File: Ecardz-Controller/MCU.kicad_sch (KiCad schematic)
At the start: 31 parts, among them J1 MEM2061-01-188-00-A, J2 Conn_01x04, J3 Conn_01x05, U1 STM32G0C1RETx

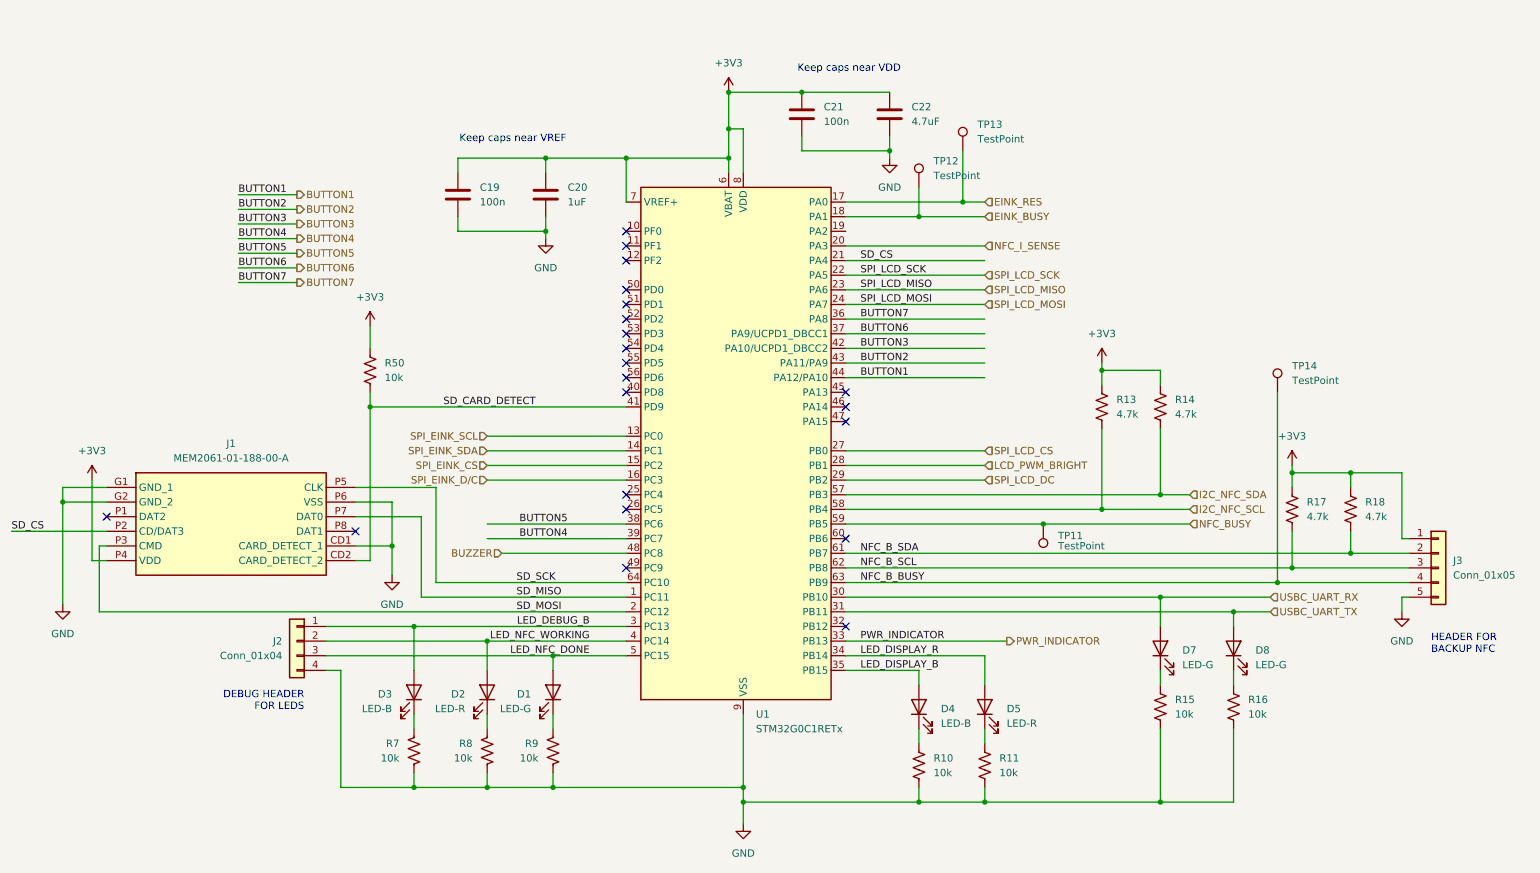
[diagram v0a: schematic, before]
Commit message: redid MCU connections from IOC file from FW team
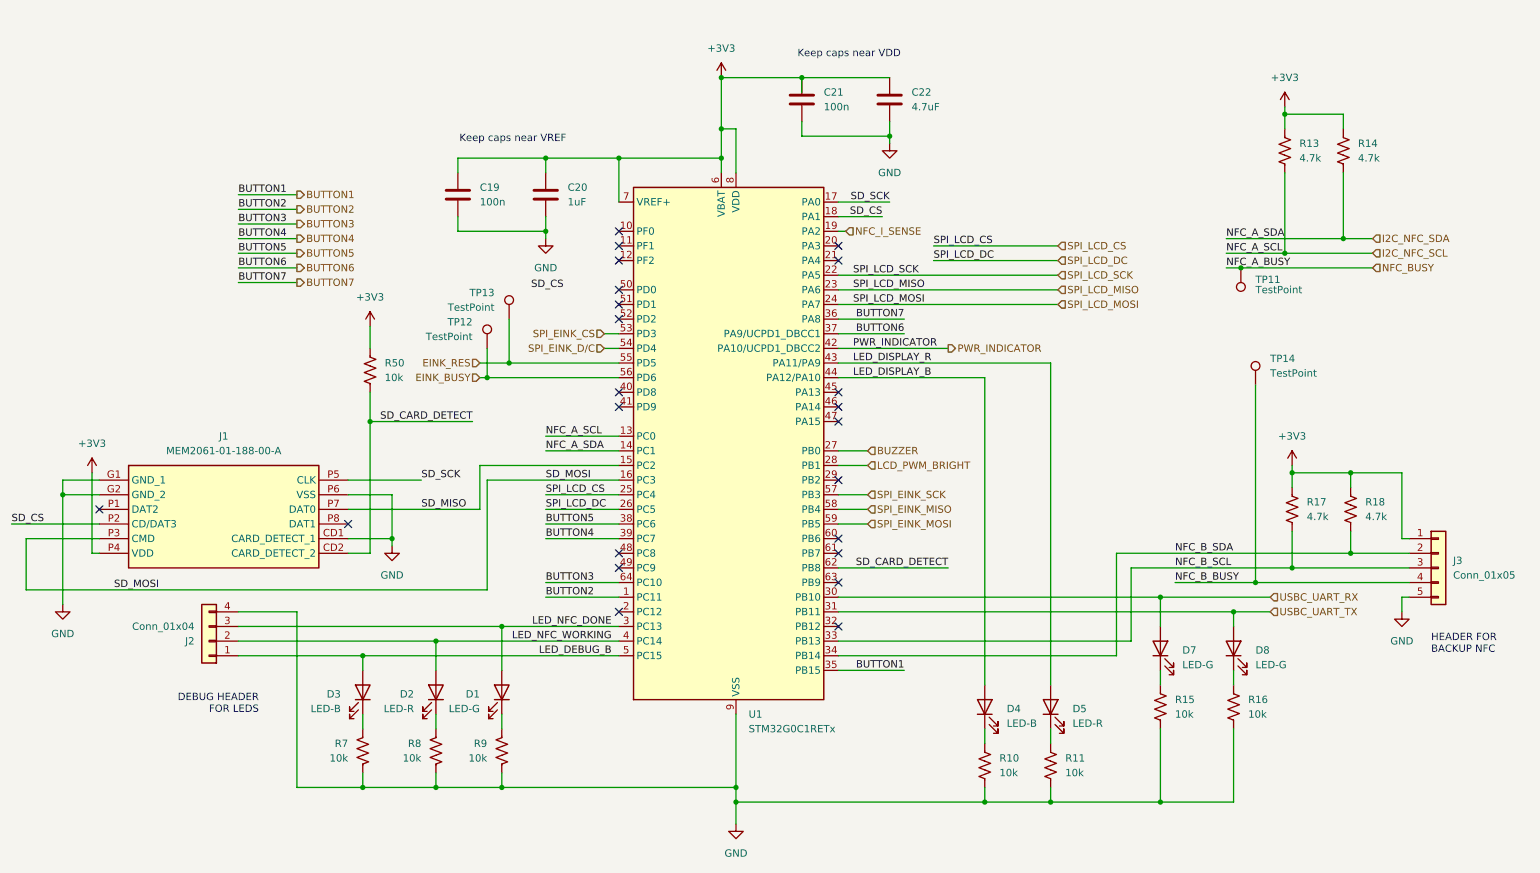
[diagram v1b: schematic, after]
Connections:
- net SPI_EINK_SCL is gone; now on net I2C_NFC_SCL: U1.13 (PC0)
- net SPI_EINK_SDA is gone; now on net I2C_NFC_SDA: U1.14 (PC1)
- net BUTTON1: now also U1.35 (PB15); no longer U1.44 (PA12/PA10)
- net BUTTON2: now also U1.1 (PC11); no longer U1.43 (PA11/PA9)
- net BUTTON3: now also U1.64 (PC10); no longer U1.42 (PA10/UCPD1_DBCC2)
- net BUZZER: now also U1.27 (PB0); no longer U1.48 (PC8)
- net EINK_BUSY: now also U1.56 (PD6); no longer U1.18 (PA1)
- net EINK_RES: now also U1.55 (PD5); no longer U1.17 (PA0)
- net I2C_NFC_SCL: no longer U1.58 (PB4)
- net I2C_NFC_SDA: no longer U1.57 (PB3)
- net LED_DEBUG_B: now also U1.5 (PC15); no longer U1.3 (PC13)
- net LED_DISPLAY_B: now also U1.44 (PA12/PA10); no longer U1.35 (PB15)
- net LED_DISPLAY_R: now also U1.43 (PA11/PA9); no longer U1.34 (PB14)
- net LED_NFC_DONE: now also U1.3 (PC13); no longer U1.5 (PC15)
- net NFC_BUSY: no longer U1.59 (PB5)
- net NFC_B_BUSY: no longer U1.63 (PB9)
- net NFC_B_SCL: now also U1.33 (PB13); no longer U1.62 (PB8)
- net NFC_B_SDA: now also U1.34 (PB14); no longer U1.61 (PB7)
- net NFC_I_SENSE: now also U1.19 (PA2); no longer U1.20 (PA3)
- net PWR_INDICATOR: now also U1.42 (PA10/UCPD1_DBCC2); no longer U1.33 (PB13)
- net SD_CARD_DETECT: now also U1.62 (PB8); no longer U1.41 (PD9)
- net SD_CS: now also U1.18 (PA1); no longer U1.21 (PA4)
- net SD_MISO: now also U1.15 (PC2); no longer U1.1 (PC11)
- net SD_MOSI: now also U1.16 (PC3); no longer U1.2 (PC12)
- net SD_SCK: now also U1.17 (PA0); no longer U1.64 (PC10)
- net SPI_EINK_CS: now also U1.53 (PD3); no longer U1.15 (PC2)
- net SPI_EINK_D/C: now also U1.54 (PD4); no longer U1.16 (PC3)
- net SPI_LCD_CS: now also U1.25 (PC4); no longer U1.27 (PB0)
- net SPI_LCD_DC: now also U1.26 (PC5); no longer U1.29 (PB2)
- new net SPI_EINK_MISO: U1.58 (PB4)
- new net SPI_EINK_MOSI: U1.59 (PB5)
- new net SPI_EINK_SCK: U1.57 (PB3)
- no-connect marks 21 -> 23
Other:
- moved on the sheet: C21, C22, D1, D2, D3, D4, D5, J1, R10, R11, R13, R14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

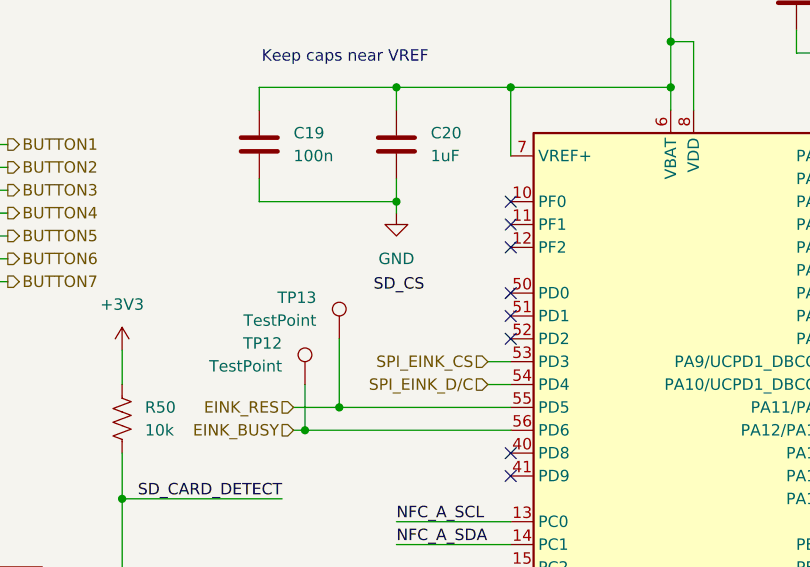
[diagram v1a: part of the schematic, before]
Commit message: updated layout for new mcu pin assignments
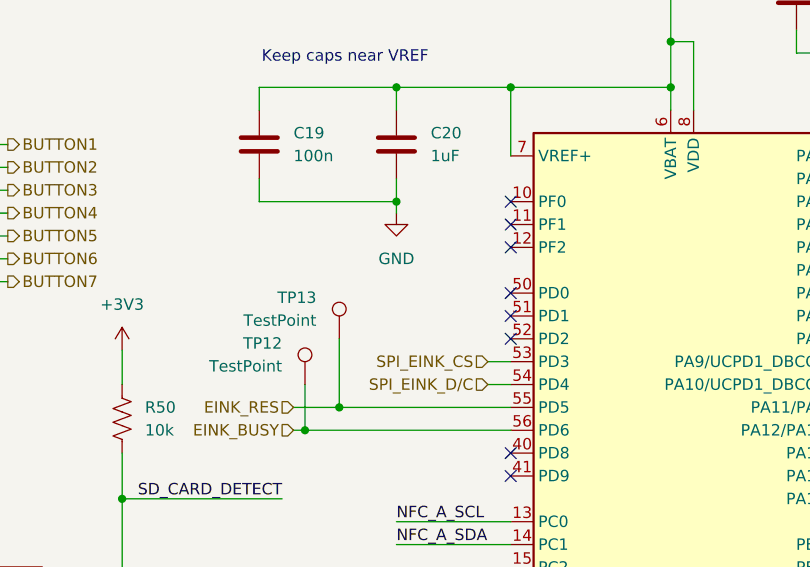
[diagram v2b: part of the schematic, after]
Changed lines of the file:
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@@
-		)
-	)
-	(label "SD_CS"
-		(at 106.68 60.96 0)
-		(fields_autoplaced yes)
-		(effects
-			(font
-				(size 1.27 1.27)
-			)
-			(justify left bottom)
 		)
 	)

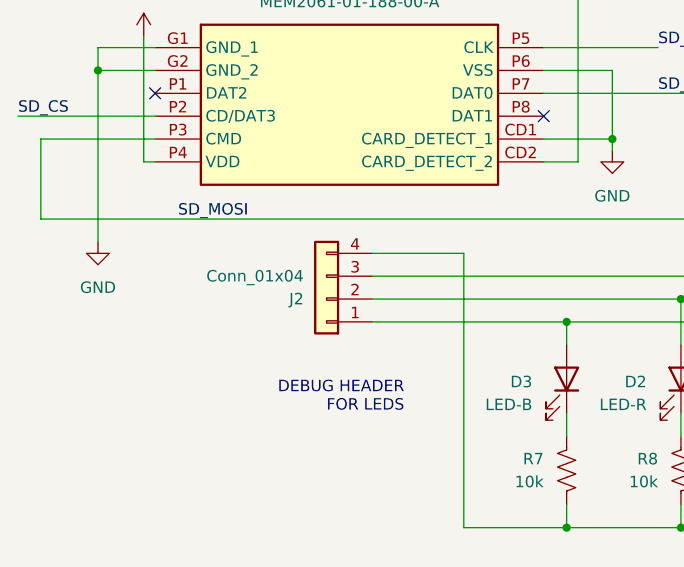
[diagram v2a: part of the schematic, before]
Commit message: changed headers to 90 degree angled headers
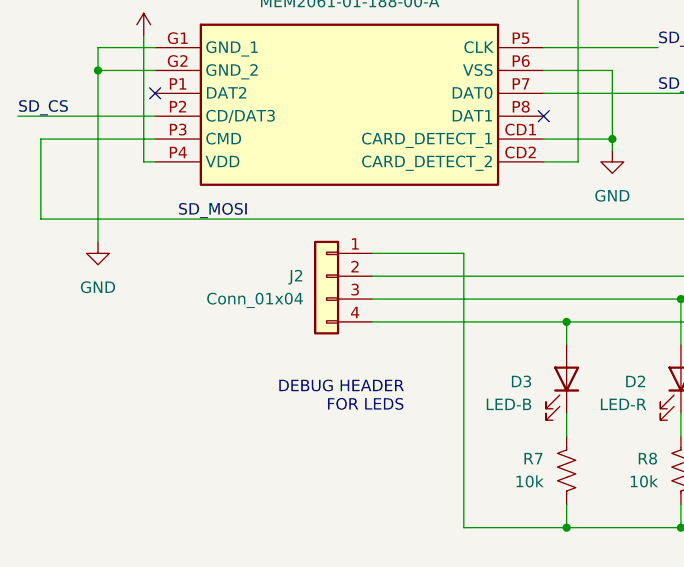
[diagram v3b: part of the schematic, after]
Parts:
- J2: footprint Connector_PinHeader_2.54mm:PinHeader_1x04_P2.54mm_Vertical -> Connector_PinHeader_2.54mm:PinHeader_1x04_P2.54mm_Horizontal
- J3: footprint Connector_PinHeader_2.54mm:PinHeader_1x05_P2.54mm_Vertical -> Connector_PinHeader_2.54mm:PinHeader_1x05_P2.54mm_Horizontal
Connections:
- net GND: now also J2.1 (Pin_1); no longer J2.4 (Pin_4)
- net LED_DEBUG_B: now also J2.4 (Pin_4); no longer J2.1 (Pin_1)
- net LED_NFC_DONE: now also J2.2 (Pin_2); no longer J2.3 (Pin_3)
- net LED_NFC_WORKING: now also J2.3 (Pin_3); no longer J2.2 (Pin_2)
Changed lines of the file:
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@@
+	)
+	(symbol
+		(lib_id "Connector_Generic:Conn_01x04")
+		(at 50.8 119.38 0)
+		(mirror y)
+		(unit 1)
+		(exclude_from_sim no)
+		(in_bom yes)
+		(on_board yes)
+		(dnp no)
+		(property "Reference" "J2"
+			(at 48.26 119.3799 0)
+			(effects
+				(font
+					(size 1.27 1.27)
+				)
+				(justify left)
+			)
+		)
+		(property "Value" "Conn_01x04"
+			(at 48.26 121.9199 0)
+			(effects
+				(font
+					(size 1.27 1.27)
+				)
+				(justify left)
+			)
+		)
+		(property "Footprint" "Connector_PinHeader_2.54mm:PinHeader_1x04_P2.54mm_Horizontal"
+			(at 50.8 119.38 0)
+			(effects
+				(font
+					(size 1.27 1.27)
+				)
+				(hide yes)
+			)
+		)
+		(property "Datasheet" ""
+			(at 50.8 119.38 0)
+			(effects
+				(font
+					(size 1.27 1.27)
+				)
+				(hide yes)
+			)
+		)
+		(property "Description" "Generic connector, single row, 01x04, script generated (kicad-library-utils/schlib/autogen/connector/)"
+			(at 50.8 119.38 0)
+			(effects
+				(font
+					(size 1.27 1.27)
+				)
+				(hide yes)
+			)
+		)
+		(property "Part Number" "61300411121"
+			(at 50.8 119.38 0)
+			(effects
+				(font
+					(size 1.27 1.27)
+				)
+				(hide yes)
+			)
+		)
+		(pin "2"
+		)
+		(pin "3"
+		)
+		(pin "4"
+		)
+		(pin "1"
+		)
+		(instances
+			(project "Ecardz-Controller"
+				(path "/74270717-a116-451e-ac88-5a07ab66056e/24ee7b4c-70f3-405d-afd9-1146a9b5f360"
+					(reference "J2")
+					(unit 1)
+				)
+			)
+		)
 	)
 	(symbol
@@
 				(path "/74270717-a116-451e-ac88-5a07ab66056e/24ee7b4c-70f3-405d-afd9-1146a9b5f360"
 					(reference "D8")
-					(unit 1)
-				)
-			)
-		)
-	)
-	(symbol
-		(lib_id "Connector_Generic:Conn_01x04")
-		(at 50.8 121.92 180)
-		(unit 1)
-		(exclude_from_sim no)
-		(in_bom yes)
-		(on_board yes)
-		(dnp no)
-		(property "Reference" "J2"
-			(at 48.26 121.9201 0)
-			(effects
-				(font
-					(size 1.27 1.27)
-				)
-				(justify left)
-			)
-		)
-		(property "Value" "Conn_01x04"
-			(at 48.26 119.3801 0)
-			(effects
-				(font
-					(size 1.27 1.27)
-				)
-				(justify left)
-			)
-		)
-		(property "Footprint" "Connector_PinHeader_2.54mm:PinHeader_1x04_P2.54mm_Vertical"
-			(at 50.8 121.92 0)
-			(effects
-				(font
-					(size 1.27 1.27)
-				)
-				(hide yes)
-			)
-		)
-		(property "Datasheet" ""
-			(at 50.8 121.92 0)
-			(effects
-				(font
-					(size 1.27 1.27)
-				)
-				(hide yes)
-			)
-		)
-		(property "Description" "Generic connector, single row, 01x04, script generated (kicad-library-utils/schlib/autogen/connector/)"
-			(at 50.8 121.92 0)
-			(effects
-				(font
-					(size 1.27 1.27)
-				)
-				(hide yes)
-			)
-		)
-		(property "Part Number" "61300411121"
-			(at 50.8 121.92 0)
-			(effects
-				(font
-					(size 1.27 1.27)
-				)
-				(hide yes)
-			)
-		)
-		(pin "2"
-		)
-		(pin "3"
-		)
-		(pin "4"
-		)
-		(pin "1"
-		)
-		(instances
-			(project "Ecardz-Controller"
-				(path "/74270717-a116-451e-ac88-5a07ab66056e/24ee7b4c-70f3-405d-afd9-1146a9b5f360"
-					(reference "J2")
 					(unit 1)
 				)
@@
 			)
 		)
-		(property "Footprint" "Connector_PinHeader_2.54mm:PinHeader_1x05_P2.54mm_Vertical"
+		(property "Footprint" "Connector_PinHeader_2.54mm:PinHeader_1x05_P2.54mm_Horizontal"
 			(at 264.16 109.22 0)
 			(effects

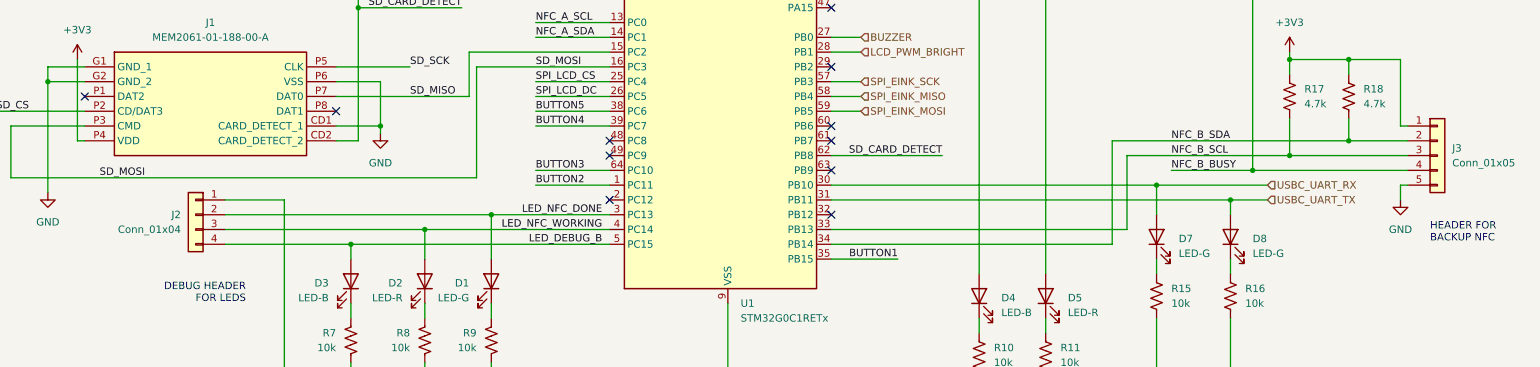
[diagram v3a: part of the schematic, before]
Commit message: moved headers to bottom of board, made J3 DNP
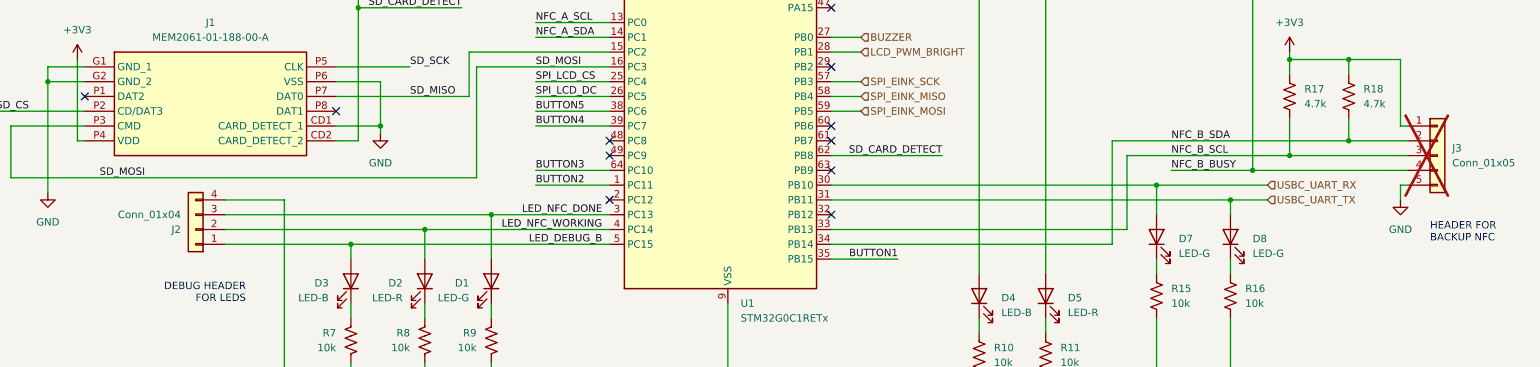
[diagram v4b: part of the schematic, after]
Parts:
- J3: now not fitted
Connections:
- net GND: now also J2.4 (Pin_4); no longer J2.1 (Pin_1)
- net LED_DEBUG_B: now also J2.1 (Pin_1); no longer J2.4 (Pin_4)
- net LED_NFC_DONE: now also J2.3 (Pin_3); no longer J2.2 (Pin_2)
- net LED_NFC_WORKING: now also J2.2 (Pin_2); no longer J2.3 (Pin_3)
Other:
- moved on the sheet: J2

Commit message: changed hole positions and fixed flex connector location in 3d model
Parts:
- added C54, C55, C56, C57, C58, C59, C60: 1uF, Capacitor_SMD:C_0603_1608Metric_Pad1.08x0.95mm_HandSolder, symbol Device:C
- added R51, R52, R53, R54, R55, R56, R57: 10k, Resistor_SMD:R_0603_1608Metric_Pad0.98x0.95mm_HandSolder, symbol Device:R_US
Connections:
- net BUTTON1: now also R51.2; no longer U1.35 (PB15)
- net BUTTON2: now also R52.2; no longer U1.1 (PC11)
- net BUTTON3: now also R53.2; no longer U1.64 (PC10)
- net BUTTON4: now also R54.2; no longer U1.39 (PC7)
- net BUTTON5: now also R55.2; no longer U1.38 (PC6)
- net BUTTON6: now also R56.2; no longer U1.37 (PA9/UCPD1_DBCC1)
- net BUTTON7: now also R57.2; no longer U1.36 (PA8)
- net GND: now also C54.2, C55.2, C56.2, C57.2, C58.2, C59.2, C60.2
- new net BUTTON_1: C54.1, R51.1, U1.35 (PB15)
- new net BUTTON_2: C55.1, R52.1, U1.1 (PC11)
- new net BUTTON_3: C56.1, R53.1, U1.64 (PC10)
- new net BUTTON_4: C57.1, R54.1, U1.39 (PC7)
- new net BUTTON_5: C58.1, R55.1, U1.38 (PC6)
- new net BUTTON_6: C59.1, R56.1, U1.37 (PA9/UCPD1_DBCC1)
- new net BUTTON_7: C60.1, R57.1, U1.36 (PA8)

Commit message: final layout before fab
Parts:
- added J11: Conn_01x02, Connector_PinHeader_2.54mm:PinHeader_1x02_P2.54mm_Horizontal, symbol Connector_Generic:Conn_01x02
- added R58: 10k, Resistor_SMD:R_0603_1608Metric_Pad0.98x0.95mm_HandSolder, symbol Device:R_US
- added R59: 4.7k, Resistor_SMD:R_0603_1608Metric_Pad0.98x0.95mm_HandSolder, symbol Device:R_US
- R17, R18: now not fitted
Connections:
- net +3V3: now also R59.1
- net GND: now also R58.2
- net NFC_BUSY: now also U1.52 (PD2), R59.2
- net USBC_UART_RX: now also J11.2 (Pin_2)
- net USBC_UART_TX: now also J11.1 (Pin_1)
- net at U1.46 (PA14): now also R58.1
- no-connect marks 23 -> 21
